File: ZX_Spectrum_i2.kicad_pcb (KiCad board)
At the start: 2 copper layers, 213.5 x 130.1 mm, 199 parts, among them IC1 ULA, IC10 4116, IC11 4116, IC12 4116, IC13 4116, IC14 LM1889, IC15 4532, IC16 4532, IC17 4532, IC18 4532, IC19 4532, IC2 Z80, IC20 4532, IC21 4532, IC22 4532, IC23 74LS32, IC24 74LS00, IC25 74LS157, IC26 74LS157, IC3 74LS157, IC4 74LS157, IC5 ROM, IC6 4116, IC7 4116, IC8 4116, IC9 4116, J1 MIC, J2 EAR, J3 EDGE CONNECTOR, J4 Barrel_Jack, T1 COIL 13/39, U1 MODULATOR, U2 L7805, X1 14MHz, X2 4.433619MHz

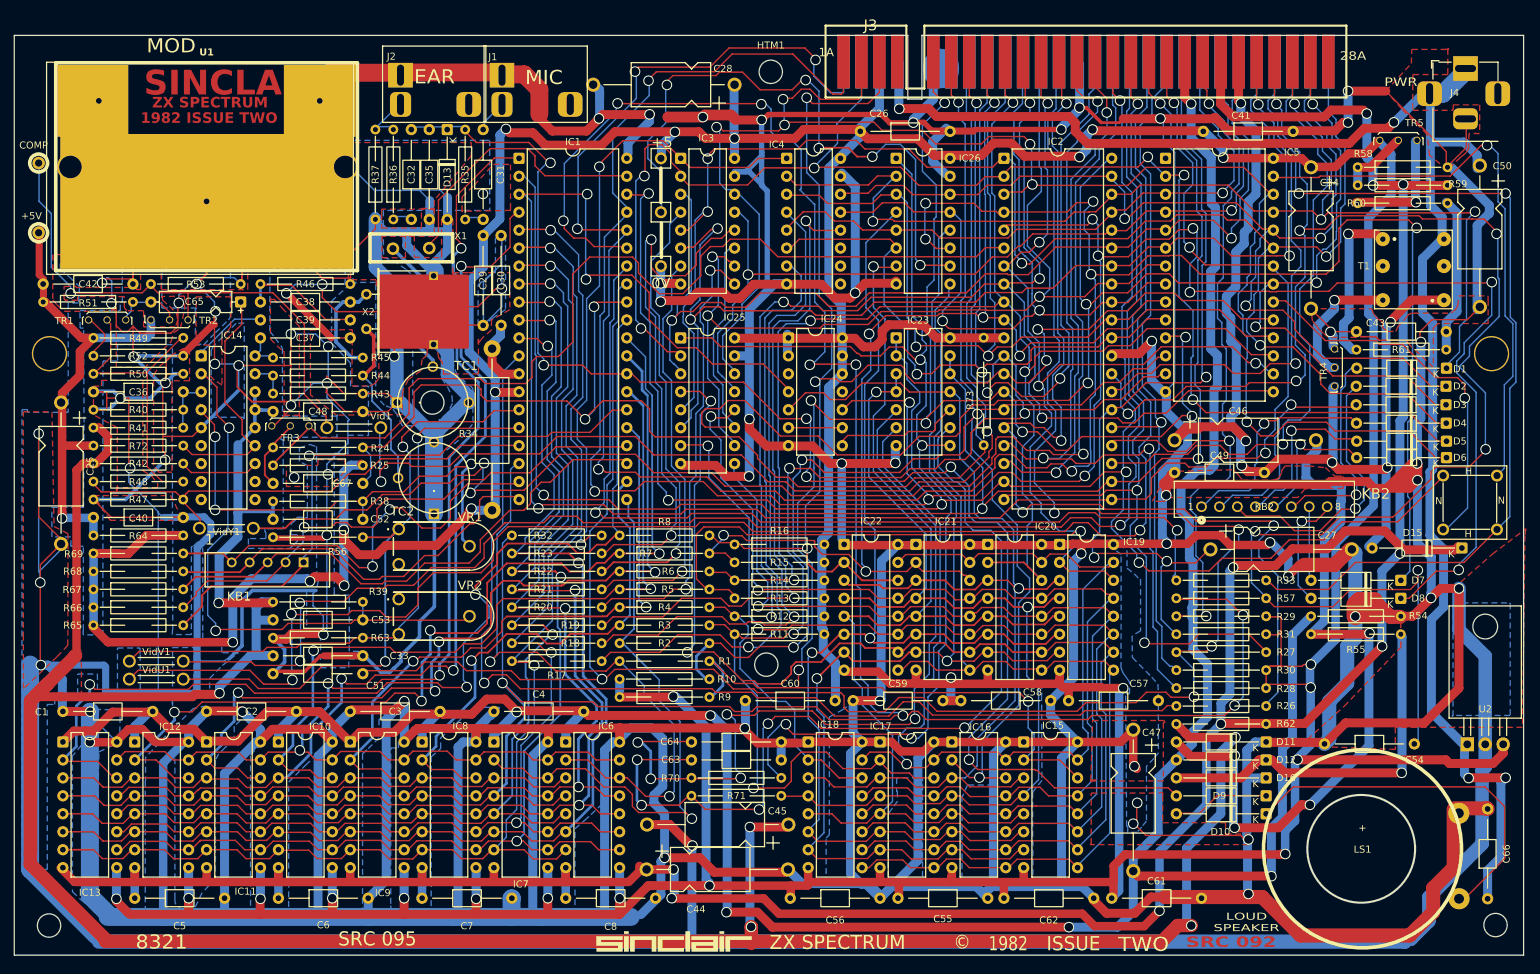
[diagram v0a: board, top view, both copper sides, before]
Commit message: Add files via upload
Updated board sizes and hole positions along with new step models.
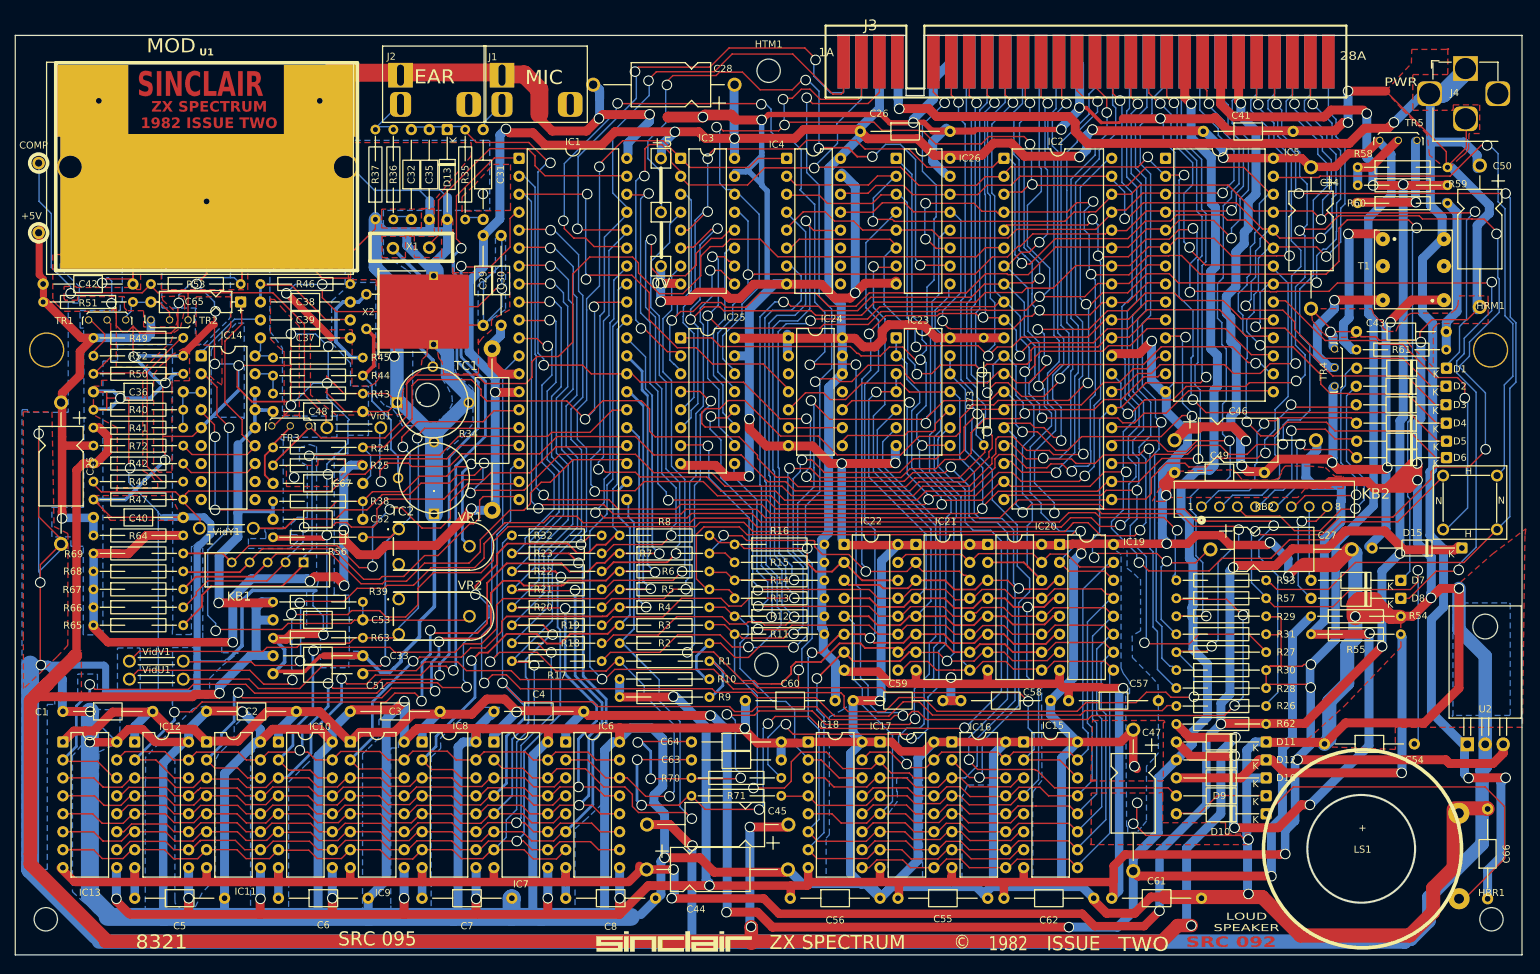
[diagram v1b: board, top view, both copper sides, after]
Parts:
- moved HTC1 1.29 mm to (100.1, 73.8)
- moved HBR1 1.00 mm to (250.6, 148.0)
- moved HBL1 1.00 mm to (46.1, 148.0)
- moved HLM1 0.66 mm to (46.2, 67.5)
- moved HRM1 0.54 mm to (250.4, 67.5)
- moved HTM1 0.34 mm to (148.3, 28.0)
- moved X1 0.07 mm to (97.9, 57.5)
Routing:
- net ~{CLK}: track 192.2 -> 193.6 mm
- net Net-(IC2-~{CPUCLK}): track 136.4 -> 137.4 mm
- net GND: track 2922.6 -> 2923.1 mm
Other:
- board size 213.5 x 130.1 mm -> 213.1 x 130 mm
